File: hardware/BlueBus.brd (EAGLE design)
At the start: 90 x 55 mm, 76 parts

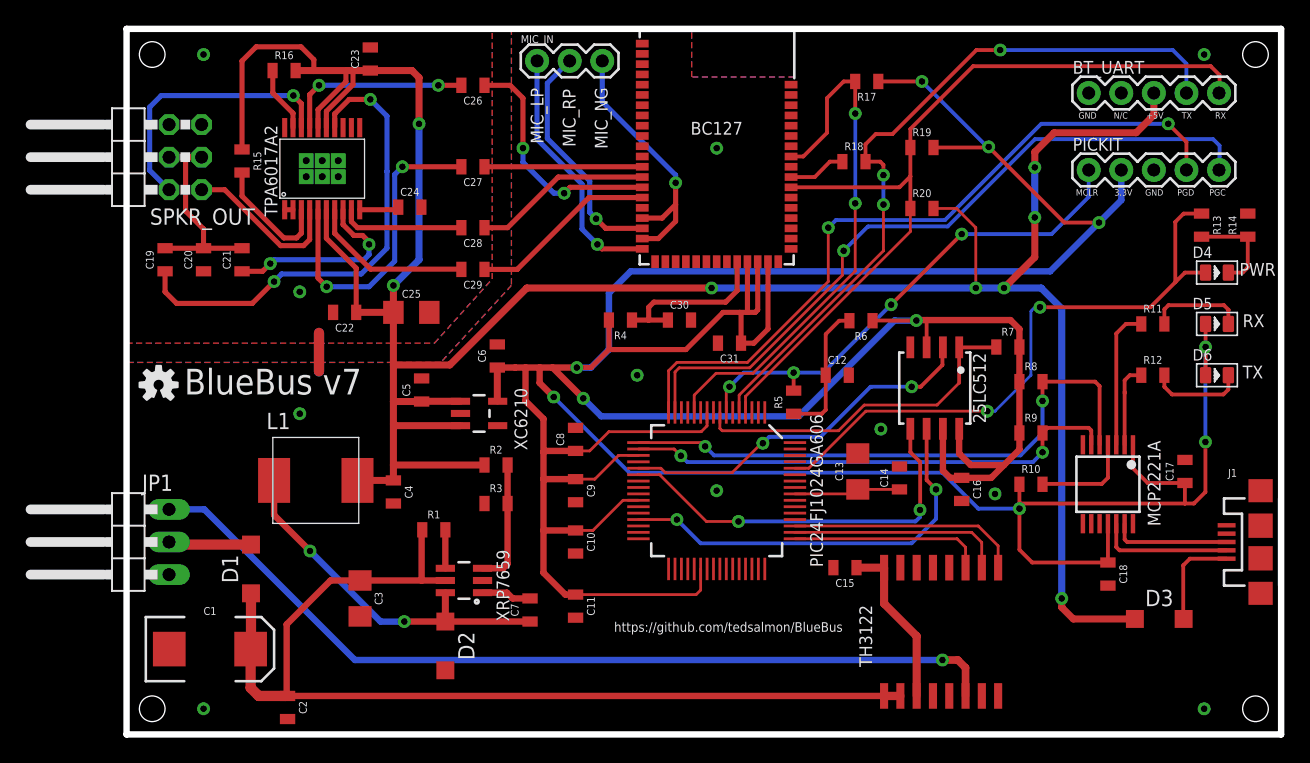
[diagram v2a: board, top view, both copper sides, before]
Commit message: [IMP] hardware: BlueBus Rev A * Remove TPA6017A2 in favor of PCM5102A Line Level DAC which will fix quality issues * Completely new layout of board and schematic * Update Silkscreen to use vector fonts of consistent sizes * Resize board to 45mm x 70mm from 55mm x 90mm * Update design of transient filter to prevent voltage drops at boot * Add DSP Output SMB connector * Add circuit for mono microphone input * Add 1.5A Littleblock Fuse to prevent over-current * Miter board corners for rounded look
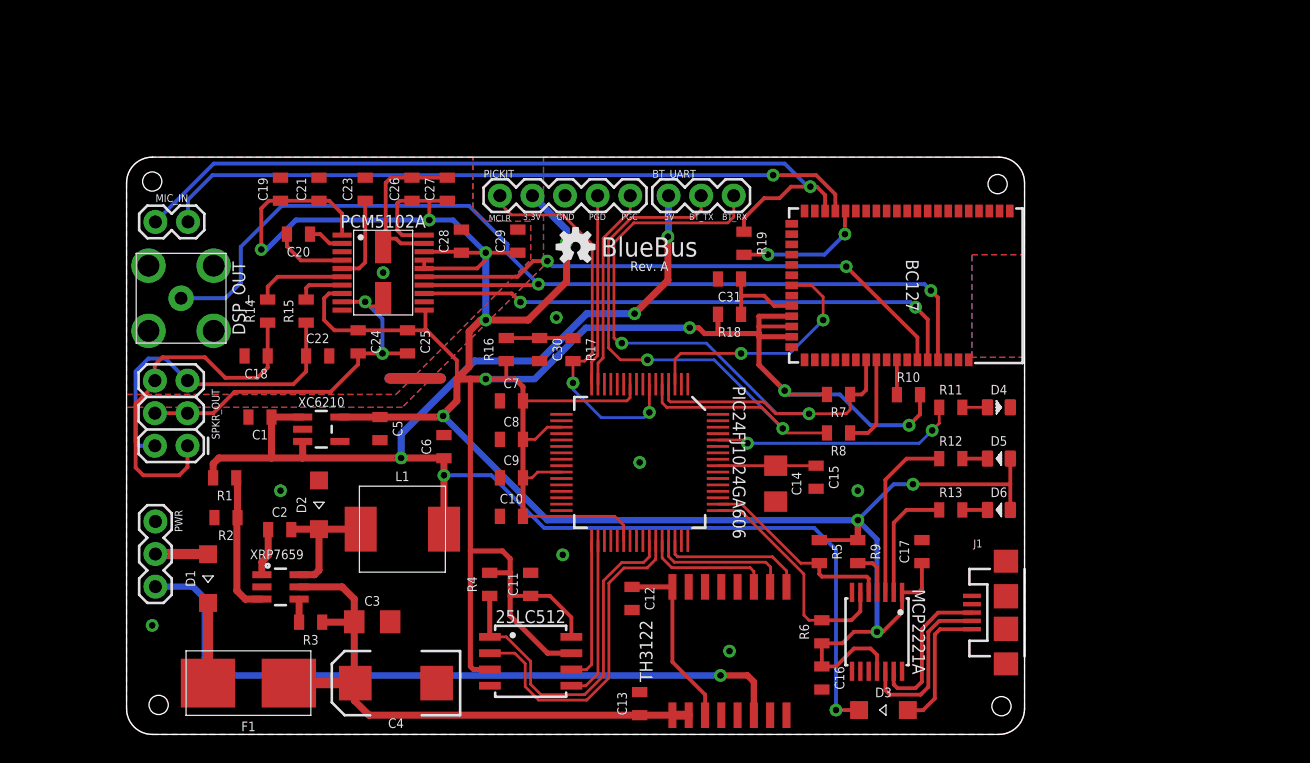
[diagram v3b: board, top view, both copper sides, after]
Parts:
- removed FRAME3: FRAME-LETTER, Frame:DUMMY
- removed JP1: (no value), pinhead:1X03/90
- removed R20: 10k, Passives:0805
- removed TPA6017A2: (no value), TPA6017A2:TSSOP20PWP
- added DSP_OUT: SMB_CONN, Connectors:MOLEX_SMB
- added F1: 1.5A, Passives:LITTLEFUSE
- added PCM5102A: PCM5102A, ICs:TSSOP20
- added PWR: (no value), SparkFun-Connectors:1X03
- added SH1, SH2: SHORTT5, shorts:SHORT_TOP-50
- BC127: value (none) -> BC127; device BC127:BC127 -> ICs:BC127
- BT_UART: device SparkFun-Connectors:1X05 -> SparkFun-Connectors:1X03
- C1: value 100uF -> 1uF; device Passives:EIA7343 -> Passives:0805
- C12: value 0.1uF -> 2.2uF
- C13: value 10uF -> 47nF; device Passives:1206 -> Passives:0805
- C14: value 0.1uF -> 10uF; device Passives:0805 -> Passives:1206
- C15: value 2.2uF -> 0.1uF
- C18: value 0.1uF -> 2.2nF
- C19: value (none) -> 10uF
- C2: value 47nF -> 0.01uF
- C20: value (none) -> 2.2uF
- C21: value (none) -> 0.1uF
- C22: value 0.47uF -> 2.2nF
- C23: value 0.47uF -> 2.2uF
- C24, C26, C28: value 0.47uF -> 0.1uF
- C25: device Passives:1206 -> Passives:0805
- C27, C29: value 0.47uF -> 10uF
- C30: value 4.7uF -> 0.1uF
- C31: value 100nF -> 4.7uF
- C4: value 22uF -> 100uF; device Passives:0805 -> Passives:EIA7343
- C6: value 2.2uF -> 22uF
- C7: value 0.01uF -> 0.1uF
- D4, D5: value GREEN-0805 -> LED_GREEN; device Seeed-LED:LED-0805 -> Passives:LED-0805
- D6: value RED-0805 -> LED_RED; device Seeed-LED:LED-0805 -> Passives:LED-0805
- MCP2221A: value (none) -> MCP2221A
- MIC_IN: device SparkFun-Connectors:1X03 -> SparkFun-Connectors:1X02
- PIC24FJ1024GA606: device PIC24FJ1024GA606:TQFP64 -> ICs:TQFP64
- R1: value 100k -> 47k
- R13: value 36k -> 1k
- R14: value 2k -> 470
- R15: value 100k -> 470
- R16, R8, R9: value 100k -> 10k
- R17: value 10k -> 240
- R18: value 10k -> 2
- R19: value 10k -> 2k
- R2: value 47k -> 9.09k
- R3: value 9.09k -> 100k
- R4: value 2k -> 5.1k
- R5: value 240 -> 100k
- R6: value 10k -> 100k
- R7: value 5.1k -> 10k
- SPKR_OUT: value (none) -> FEMALE 2x3; device pinhead:2X03/90 -> SparkFun-Connectors:2X3
- TH3122: value (none) -> TH3122.4; device TH3122_4:SOIC16DF -> ICs:SOIC16DF
- XC6210: device XC6210:SOT23-5 -> ICs:SOT23-5
- XRP7659: value (none) -> XRP7659SOT23-6; device XRP7659:SOT23-6 -> ICs:SOT23-6
- moved R14 76.7 mm to (11.0, 33.0)
- moved C18 68.5 mm to (10.1, 29.5), turned to 180 degrees
- moved PICKIT 45.9 mm to (29.1, 42.0)
- moved 25LC512 38.0 mm to (31.5, 5.70), turned to 270 degrees
- moved OSHW 34.2 mm to (35.0, 38.0)
- moved BT_UART 33.7 mm to (42.2, 42.0)
- moved MIC_IN 32.3 mm to (2.25, 40.0)
- moved R17 31.0 mm to (34.8, 30.0), turned to 270 degrees
- moved R13 29.6 mm to (64.2, 17.5), turned to 0 degrees
- moved R16 27.8 mm to (29.6, 30.0), turned to 90 degrees
- moved C13 24.8 mm to (40.0, 2.40)
- moved R6 24.4 mm to (54.2, 8.00), turned to 90 degrees
- moved C12 23.6 mm to (39.4, 10.6), turned to 270 degrees
- moved SPKR_OUT 23.1 mm to (4.75, 22.5)
- moved R4 23.0 mm to (28.3, 11.7), turned to 90 degrees
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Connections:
- net MCP_5V renamed 5V_USB
- removed net BS: C7.2, XRP7659.1
- removed net BT_RESET: BC127.44, PIC24FJ1024GA606.12, R17.2
- removed net BT_VCHG: BC127.30, C30.1, R4.1
- removed net BYP: C24.1, TPA6017A2.10
- removed net EN: R1.2, XRP7659.4
- removed net FB: R2.2, R3.2, XRP7659.3
- removed net GAIN1: R15.2, TPA6017A2.3
- removed net MCP_LED0: MCP2221A.2, R12.1
- removed net MCP_LED0_RES: D6.-, R12.2
- removed net MCP_LED1: MCP2221A.3, R11.1
- removed net MCP_LED1_RES: D5.-, R11.2
- removed net MCP_RESET: MCP2221A.4, R10.2
- removed net MCU_MCLR_PULL_UP: C12.1, R5.1, R6.2
- removed net MIC_LP: BC127.21, MIC_IN.1
- removed net MIC_NEG: BC127.18, BC127.20, MIC_IN.3
- removed net MIC_RP: BC127.19, MIC_IN.2
- removed net ON_LED: D4.+, PIC24FJ1024GA606.60, R13.1
- removed net ON_LED_RES: D4.-, R13.2, R14.1
- removed net SHDN: R16.1, TPA6017A2.19
- removed net SPKR_IN_LN: BC127.13, C27.1, C27.2, TPA6017A2.5
- removed net SPKR_IN_LP: BC127.14, C28.1, C28.2, TPA6017A2.9
- removed net SPKR_IN_RN: BC127.15, C26.1, C26.2, TPA6017A2.17
- removed net SPKR_IN_RP: BC127.16, C29.1, C29.2, TPA6017A2.7
- removed net SPKR_OUT_GND: C19.2, C20.2, C21.2, SPKR_OUT.3, SPKR_OUT.4
- removed net SPKR_OUT_LN: C21.1, TPA6017A2.8
- removed net SPKR_OUT_LP: SPKR_OUT.1, TPA6017A2.4
- removed net SPKR_OUT_RN: C19.1, TPA6017A2.14
- removed net SPKR_OUT_RP: SPKR_OUT.2, TPA6017A2.18
- removed net SW: C7.1, D2.C, L1.P$1, XRP7659.6
- removed net VCAP: C13.1, C14.1, PIC24FJ1024GA606.56
- new net 12V: D1.A, PWR.2
- new net 5VREG_BS: C2.1, XRP7659.1
- new net 5VREG_EN: R3.2, XRP7659.4
- new net 5VREG_FB: R1.1, R2.1, XRP7659.3
- new net 5VREG_SW: C2.2, D2.C, L1.P$1, XRP7659.6
- new net AGND: C24.2, C25.2, PCM5102A.9, SH1.2, SPKR_OUT.3, SPKR_OUT.4
- new net BT_3V3_FILTER: BC127.30, C31.1, R18.1
- new net BT_DCLK: BC127.47, PCM5102A.13
- new net BT_DOUT: BC127.48, DSP_OUT.P$1, PCM5102A.14
- new net BT_DWS: BC127.46, PCM5102A.15
- new net BT_MIC_BIAS: BC127.17, R19.2
- new net BT_MIC_RN: BC127.18, MIC_IN.2
- new net BT_MIC_RP: BC127.19, MIC_IN.1, R19.1
- new net BT_RST: BC127.44, R10.1
- new net BT_VREGEN: BC127.28, PIC24FJ1024GA606.3
- new net DAC_CAPM: C20.2, PCM5102A.4
- new net DAC_CAPP: C20.1, PCM5102A.2
- new net DAC_OUT_L: PCM5102A.6, R14.2
- new net DAC_OUT_R: PCM5102A.7, R15.2
- new net DAC_VNEG: C23.1, PCM5102A.5
- new net DGND: C26.2, C27.2, PCM5102A.19, SH2.2
- new net MCP_RST: MCP2221A.4, R9.2
- new net MCP_RX_LED: MCP2221A.3, R12.1
- new net MCP_RX_LED_RES: D6.-, R13.2
- new net MCP_TX_LED: MCP2221A.2, R13.1
- new net MCP_TX_LED_RES: D5.-, R12.2
- new net MCU_MCLR_RES: C30.1, R16.2, R17.1
- new net MCU_ON_LED: PIC24FJ1024GA606.60, R11.1
- new net MCU_ON_LED_RES: D4.+, R11.2
- new net MCU_VCAP: C14.1, C15.1, PIC24FJ1024GA606.56
- new net SPKR_OUT_L: C18.1, R14.1, SPKR_OUT.1, SPKR_OUT.6
- new net SPKR_OUT_R: C22.1, R15.1, SPKR_OUT.2, SPKR_OUT.5
- net 3.3V: now also C10.2, C19.1, C21.1, C24.1, C25.1, C26.1, C27.1, C28.1, C29.1, C5.1, C7.2, C8.2, C9.2, PCM5102A.1, PCM5102A.11, PCM5102A.16, PCM5102A.17, PCM5102A.18, PCM5102A.20, PCM5102A.8, R10.2, R16.1, R18.2, R5.1; no longer C10.1, C18.1, C31.1, C6.1, C8.1, C9.1, R10.1, R17.1, R19.2, R8.1
- net 5V: now also BT_UART.1, C1.1, C6.1, R1.2; no longer BT_UART.3, C22.1, C23.1, C25.1, C4.1, C5.1, R15.1, R16.2, R2.1, R20.2, TPA6017A2.15, TPA6017A2.16, TPA6017A2.6
- net BT_URX: now also BT_UART.2, R8.1, R8.2; no longer BT_UART.4, R18.1, R18.2
- net BT_UTX: now also BT_UART.3, R7.1; no longer BT_UART.5, R19.1, R20.1
- net EE_CS: now also PIC24FJ1024GA606.42, R4.1; no longer PIC24FJ1024GA606.8, R7.1
- net EE_SCK: now also PIC24FJ1024GA606.33; no longer PIC24FJ1024GA606.29
- net EE_SI: now also PIC24FJ1024GA606.34; no longer PIC24FJ1024GA606.22
- net EE_SO: now also PIC24FJ1024GA606.43; no longer PIC24FJ1024GA606.21
- net GND: now also C1.2, C10.1, C19.2, C21.2, C28.2, C29.2, C4.C, C7.1, C8.1, C9.1, D4.-, PCM5102A.10, PCM5102A.3, PWR.1, R2.2, SH1.1, SH2.1; no longer BT_UART.1, C1.C, C10.2, C2.2, C20.1, C24.2, C25.2, C4.2, C8.2, C9.2, JP1.1, R14.2, R3.1, TPA6017A2.1, TPA6017A2.11, TPA6017A2.12, TPA6017A2.13, TPA6017A2.2, TPA6017A2.20, TPA6017A2.P$1, TPA6017A2.P$2, TPA6017A2.P$3, TPA6017A2.P$4, TPA6017A2.P$5, TPA6017A2.P$6
- net IBUS: now also PWR.3; no longer JP1.3
- net IBUS_URX: now also PIC24FJ1024GA606.45; no longer PIC24FJ1024GA606.50
- net IBUS_USTA: now also PIC24FJ1024GA606.46; no longer PIC24FJ1024GA606.51
- net IBUS_UTX: now also PIC24FJ1024GA606.44; no longer PIC24FJ1024GA606.49
- net MCU_MCLR: now also R17.2; no longer R5.2
- net SYS_URX: now also PIC24FJ1024GA606.50, R5.2; no longer PIC24FJ1024GA606.17, R8.2
- net SYS_UTX: now also PIC24FJ1024GA606.49, R6.2; no longer PIC24FJ1024GA606.18, R9.2
- net VIN: now also C13.1, C4.A, F1.IN, F1.OUT, R3.1; no longer C1.A, C2.1, D1.A, JP1.2, R1.1
- net VTR: now also C12.1; no longer C15.1
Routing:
- net 5V: track 216.4 -> 113.2 mm, vias 8 -> 5
- net BT_DOUT: track 0.00 -> 80.8 mm, vias 0 -> 2
- net BT_MIC_RP: track 0.00 -> 63.6 mm, vias 0 -> 1
- net BT_MIC_RN: track 0.00 -> 54.9 mm, vias 0 -> 1
- net ON_LED: track 48.3 -> 0.00 mm, vias 2 -> 0
- net BT_DCLK: track 0.00 -> 43.2 mm, vias 0 -> 2
- net BT_DWS: track 0.00 -> 43.2 mm, vias 0 -> 2
- net MCU_PGD: track 56.8 -> 14.9 mm, vias 2 -> 0
- net BT_RESET: track 41.7 -> 0.00 mm, vias 2 -> 0
- net MCU_PGC: track 56.3 -> 15.7 mm, vias 1 -> 0
- net SPKR_OUT_RN: track 37.5 -> 0.00 mm, vias 2 -> 0
- net SPKR_IN_LN: track 36.9 -> 0.00 mm, vias 2 -> 0
- net VIN: track 88.1 -> 53.1 mm
- net SPKR_IN_RN: track 33.6 -> 0.00 mm, vias 4 -> 0
- net SYS_URX: track 45.8 -> 15.7 mm, vias 2 -> 0
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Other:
- board size 90 x 55 mm -> 70 x 45 mm
- board text added: "+"
- board text added: "-"
- board text added: "12V"
- board text added: "5V"
- board text added: "BT_RX"
- board text added: "BT_TX"
- board text added: "BlueBus"
- board text added: "Rev. A"
- board text removed: "+5V"
- board text removed: "BlueBus v7"
- board text removed: "L+"
- board text removed: "MIC_LP"
- board text removed: "MIC_NG"
- board text removed: "MIC_RP"
- board text removed: "N/C"
- board text removed: "NEG"
- board text removed: "PWR"
- board text removed: "R+"
- board text removed: "RX"
- board text removed: "TX"
- board text removed: "VIN"
- board text removed: "https://github.com/tedsalmon/BlueBus"

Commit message: [IMP] hardware: BlueBus Rev A * Improve Silkscreen * Rewire a couple of nets to reduce via count * Move passives into better alignment
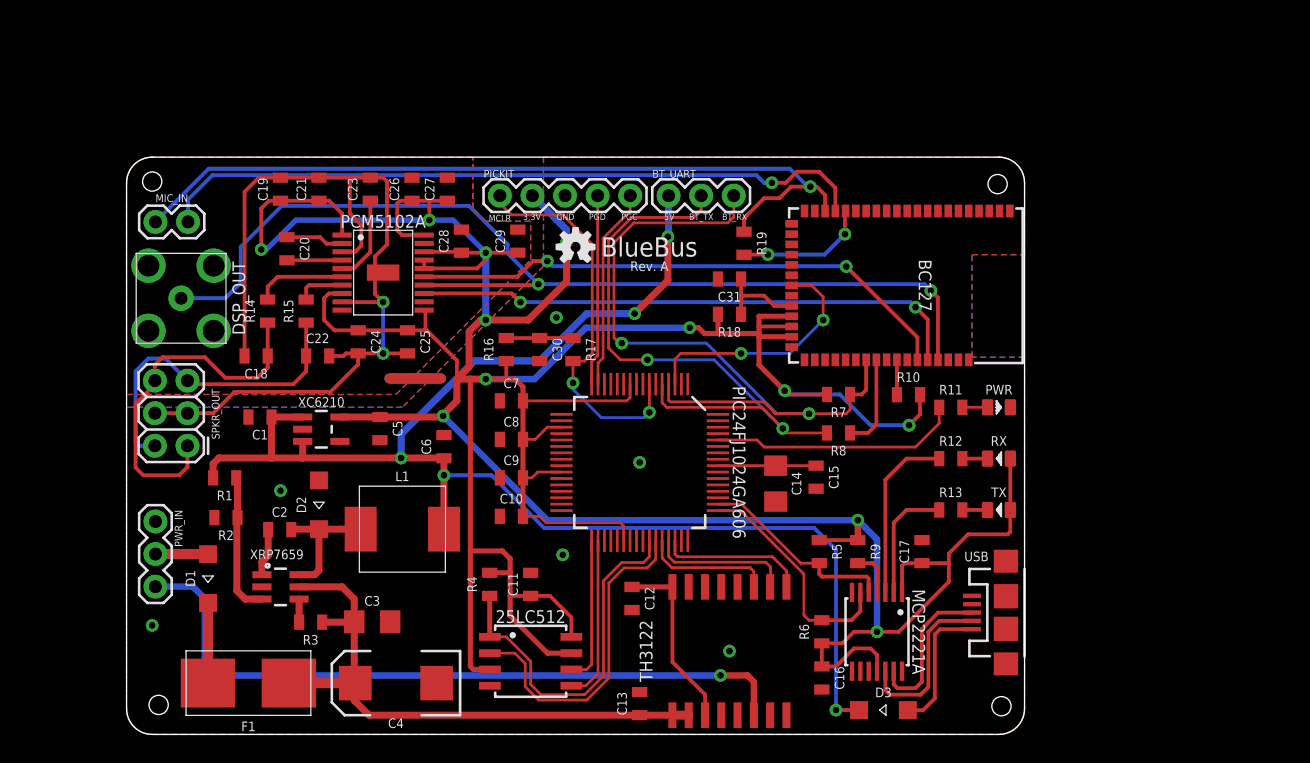
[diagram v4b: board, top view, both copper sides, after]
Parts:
- removed D4: LED_GREEN, Passives:LED-0805
- removed SH2: SHORTT5, shorts:SHORT_TOP-50
- added PWR_IN: (no value), SparkFun-Connectors:1X03
- PWR: value (none) -> LED_GREEN; device SparkFun-Connectors:1X03 -> Passives:LED-0805
- moved PWR 66.3 mm to (68.0, 25.5), turned to 0 degrees
- moved SH1 2.00 mm to (20.0, 36.0), turned to 0 degrees
- moved C20 1.45 mm to (12.5, 37.9), turned to 270 degrees
- moved C23 0.40 mm to (19.0, 42.5)
- renumbered D5 to RX, D6 to TX, J1 to USB
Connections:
- removed net DGND: C26.2, C27.2, PCM5102A.19, SH2.2
- net 12V: now also PWR_IN.2; no longer PWR.2
- net AGND: now also C18.2, C19.2, C21.2, C22.2, C23.2, PCM5102A.3
- net GND: now also C26.2, C27.2, PCM5102A.19, PWR.-, PWR_IN.1; no longer C18.2, C19.2, C21.2, C22.2, C23.2, D4.-, PCM5102A.3, PWR.1, SH2.1
- net IBUS: now also PWR_IN.3; no longer PWR.3
- net MCU_ON_LED_RES: now also PWR.+; no longer D4.+
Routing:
- net AGND: track 30.1 -> 73.6 mm
- net DGND: track 12.8 -> 0.00 mm
- net DAC_CAPP: track 2.80 -> 4.52 mm
- net 3.3V: track 342.4 -> 343.9 mm, vias 13 -> 12
- net DAC_CAPM: track 5.72 -> 4.31 mm
- net BT_MIC_RN: track 54.9 -> 55.9 mm
- net MCU_ON_LED: track 19.2 -> 19.5 mm, vias 2 -> 0
- net GND: vias 7 -> 5

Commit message: [IMP] hardware: BlueBus Rev A * Improve Silkscreen * Rewire a couple of nets to reduce via count * Move passives into better alignment
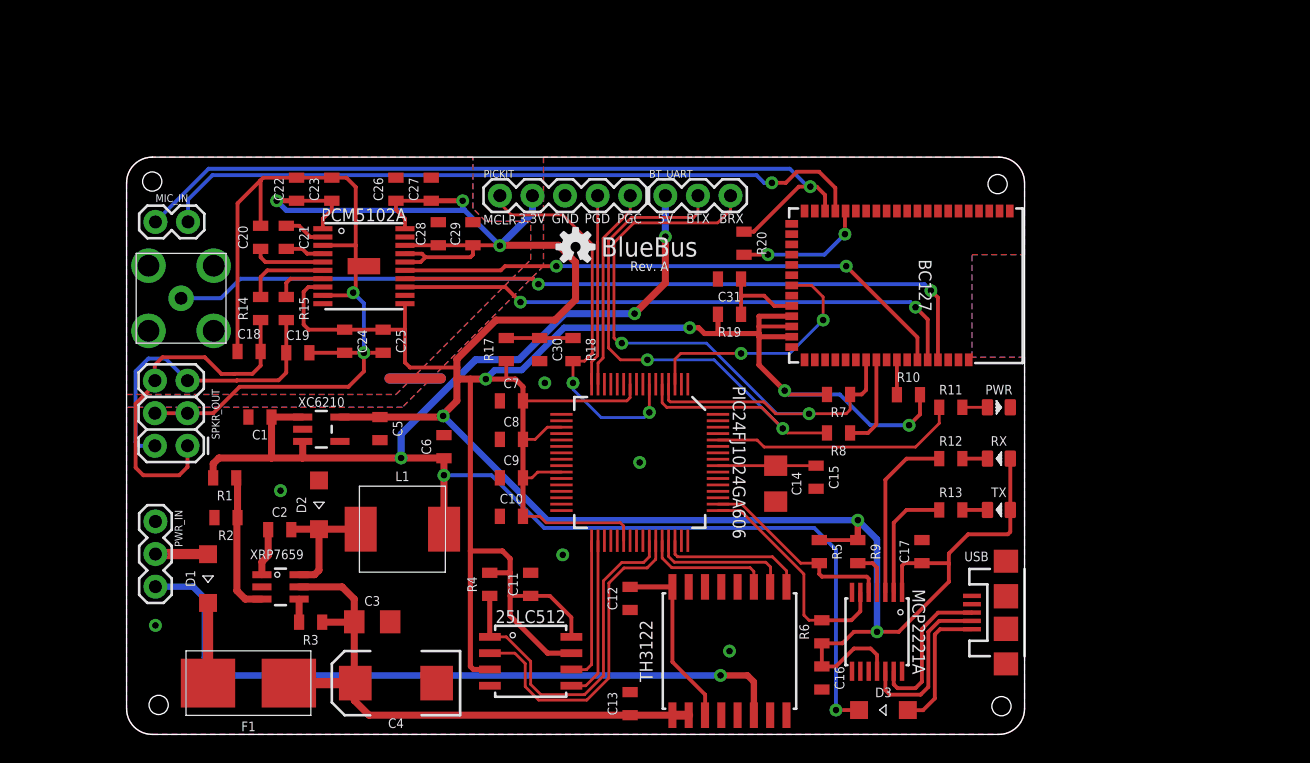
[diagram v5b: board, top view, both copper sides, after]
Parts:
- removed R16: 10k, Passives:0805
- added R20: 2k, Passives:0805
- C19: value 10uF -> 2.2nF
- C21: value 0.1uF -> 2.2uF
- C22: value 2.2nF -> 10uF
- C23: value 2.2uF -> 0.1uF
- R17: value 240 -> 10k
- R18: value 2 -> 240
- R19: value 2k -> 2
- moved C22 13.1 mm to (13.2, 42.5), turned to 90 degrees
- moved C19 12.8 mm to (13.3, 29.8), turned to 0 degrees
- moved R18 12.5 mm to (34.8, 30.0), turned to 270 degrees
- moved R19 5.65 mm to (47.0, 32.8), turned to 180 degrees
- moved R17 5.20 mm to (29.6, 30.0), turned to 90 degrees
- moved C21 4.53 mm to (12.4, 38.8), turned to 270 degrees
- moved C29 3.55 mm to (27.0, 39.0)
- moved C23 3.00 mm to (16.0, 42.5)
- moved C20 2.23 mm to (10.4, 38.8), turned to 90 degrees
- moved C25 1.90 mm to (20.0, 30.6)
- moved C28 1.89 mm to (24.3, 39.0)
- moved PCM5102A 1.58 mm to (18.5, 36.5)
- moved SH1 1.58 mm to (18.5, 36.5)
- moved R15 1.56 mm to (12.4, 33.2)
- moved C26 1.25 mm to (21.0, 42.5)
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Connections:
- net BT_DCLK renamed BT_CLK
- net BT_DWS renamed BT_LRCK
- net 3.3V: now also C22.1, C23.1, R17.1, R19.2; no longer C19.1, C21.1, R16.1, R18.2
- net AGND: now also C20.2; no longer C21.2
- net BT_3V3_FILTER: now also R19.1; no longer R18.1
- net BT_MIC_BIAS: now also R20.2; no longer R19.2
- net BT_MIC_RP: now also R20.1; no longer R19.1
- net DAC_CAPM: now also C21.2; no longer C20.2
- net DAC_CAPP: now also C21.1; no longer C20.1
- net DAC_VNEG: now also C20.1; no longer C23.1
- net GND: now also PCM5102A.12
- net MCU_MCLR: now also R18.2; no longer R17.2
- net MCU_MCLR_RES: now also R17.2, R18.1; no longer R16.2, R17.1
- net SPKR_OUT_R: now also C19.1; no longer C22.1
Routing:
- net BT_DOUT: track 80.8 -> 75.7 mm
- net AGND: track 73.6 -> 68.6 mm
- net BT_CLK: track 43.2 -> 44.9 mm
- net SPKR_OUT_R: track 25.9 -> 24.4 mm
- net 3.3V: track 343.9 -> 342.4 mm, vias 12 -> 10
- net DAC_CAPM: track 4.31 -> 3.01 mm
- net DAC_CAPP: track 4.52 -> 3.21 mm
- net DAC_VNEG: track 6.73 -> 5.66 mm
- net BT_LRCK: track 43.2 -> 44.1 mm
- net SPKR_OUT_L: track 28.4 -> 27.7 mm
- net BT_MIC_RP: track 63.3 -> 62.6 mm
- net BT_UTX: track 57.8 -> 57.2 mm
- net DAC_OUT_L: track 7.12 -> 6.62 mm
- net GND: vias 5 -> 6
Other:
- board text added: "BRX"
- board text added: "BTX"
- board text removed: "BT_RX"
- board text removed: "BT_TX"

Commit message: [IMP] hardware: PCM5102AQ1 fixes * Remove +3.3 from LDOO caps * Wire XSMT & FMT back to +3.3 * Rewire feedback pin of +5v switching regulator
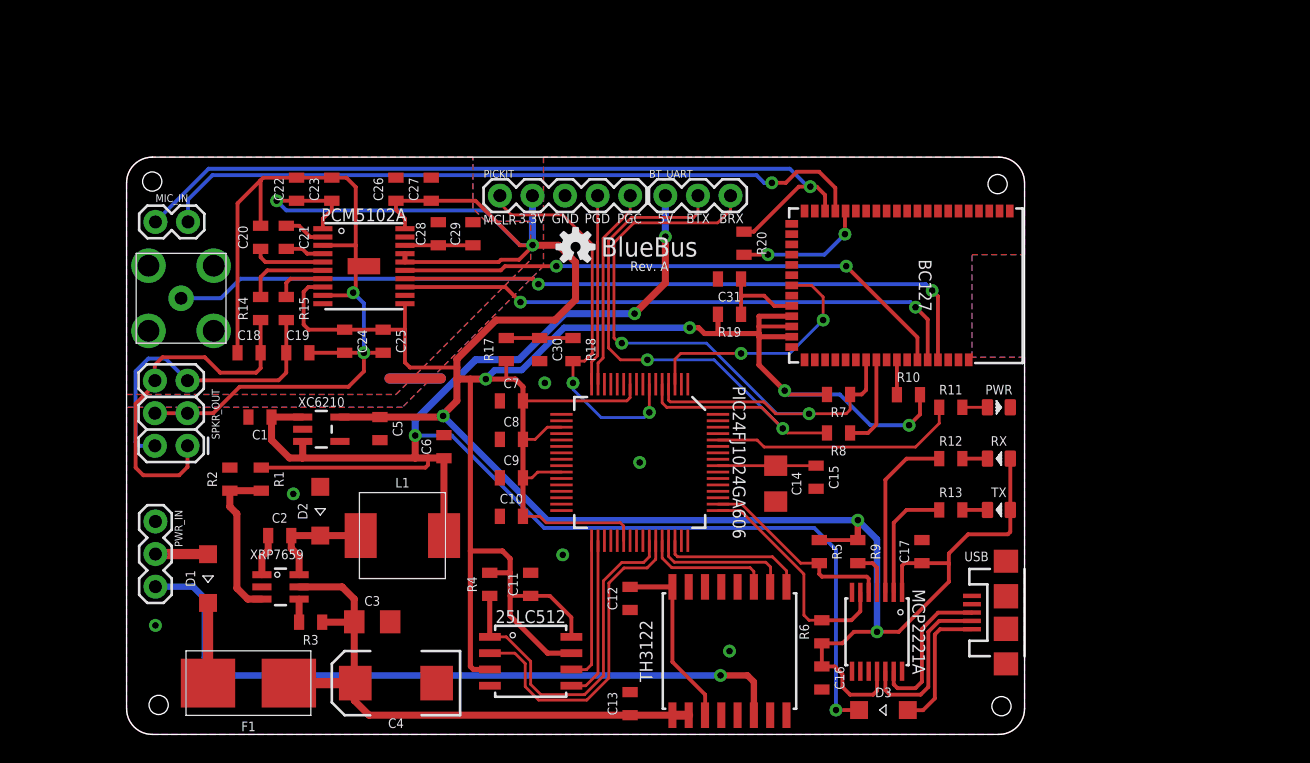
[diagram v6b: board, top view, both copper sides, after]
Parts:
- moved R2 3.01 mm to (8.05, 19.9), turned to 90 degrees
- moved R1 2.85 mm to (10.5, 19.9), turned to 90 degrees
- moved D2 0.51 mm to (15.1, 17.4)
- moved L1 0.50 mm to (21.5, 15.5)
- moved C2 0.46 mm to (11.9, 15.5)
- moved C18 0.10 mm to (9.55, 29.8)
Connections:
- new net LDOO: C28.1, C29.1, PCM5102A.18
- net 3.3V: no longer C28.1, C29.1, PCM5102A.18
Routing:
- net 5V: track 113.1 -> 123.7 mm, vias 5 -> 4
- net LDOO: track 0.00 -> 5.30 mm
- net 3.3V: track 342.4 -> 344.3 mm, vias 10 -> 9
- net 5VREG_SW: track 10.3 -> 8.71 mm
- net 5VREG_FB: track 11.1 -> 12.6 mm
